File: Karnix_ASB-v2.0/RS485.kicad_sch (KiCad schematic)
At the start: 11 parts, among them U9 MAX487ECSA+

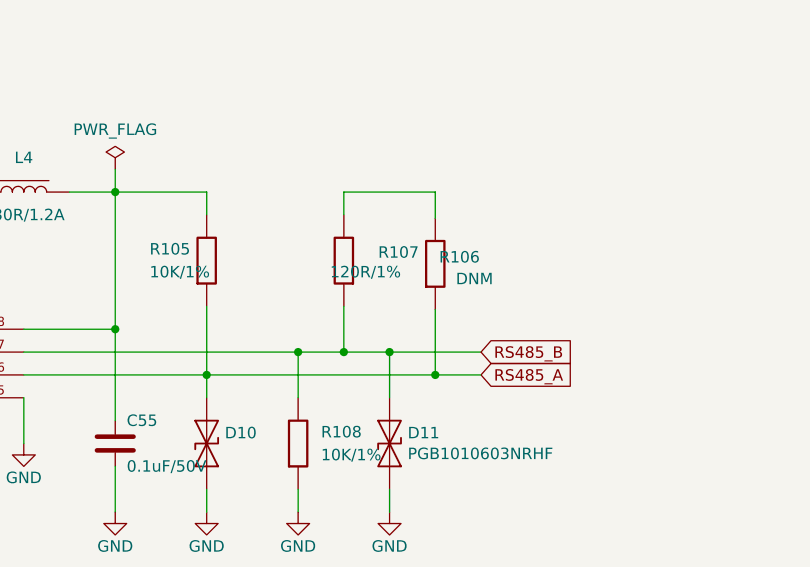
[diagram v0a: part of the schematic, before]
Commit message: V2.0 routing work in progress:
Completed parts:
1. SD-card
2. USB type A connector
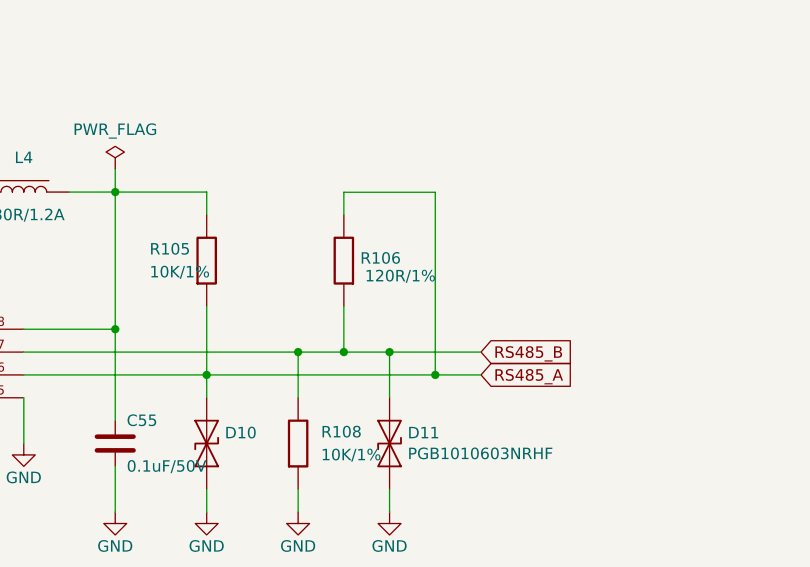
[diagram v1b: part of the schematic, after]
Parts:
- removed R107: DNM, Resistor_SMD:R_0402_1005Metric, symbol Fabmicro:Resistor
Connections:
- net RS485_A: now also R106.1
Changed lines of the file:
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@@
 	(wire
 		(pts
-			(xy 208.026 108.331) (xy 208.026 105.791)
+			(xy 208.026 108.331) (xy 208.026 105.8143)
 		)
 		(stroke
@@
 	(wire
 		(pts
-			(xy 218.186 118.8487) (xy 218.186 126.111)
+			(xy 218.186 105.8143) (xy 218.186 126.111)
 		)
 		(stroke
@@
 	(wire
 		(pts
-			(xy 208.026 105.791) (xy 218.186 105.791)
+			(xy 208.026 105.8143) (xy 218.186 105.8143)
 		)
 		(stroke
@@
 		(pts
 			(xy 177.546 105.791) (xy 182.626 105.791)
-		)
-		(stroke
-			(width 0)
-			(type default)
-		)
-	)
-	(wire
-		(pts
-			(xy 218.186 105.791) (xy 218.186 108.6887)
 		)
 		(stroke
@@
 		(dnp no)
 		(property "Reference" "R106"
-			(at 223.139 113.03 90)
+			(at 214.376 113.157 90)
 			(show_name no)
 			(do_not_autoplace no)
@@
 		)
 		(property "Value" "120R/1%"
-			(at 214.376 114.681 90)
+			(at 218.2495 115.1255 90)
 			(show_name no)
 			(do_not_autoplace no)
@@
 					(unit 1)
 				)
-			)
-		)
-	)
-	(symbol
-		(lib_id "Fabmicro:Resistor")
-		(at 218.186 113.7687 270)
-		(unit 1)
-		(body_style 1)
-		(exclude_from_sim no)
-		(in_bom yes)
-		(on_board yes)
-		(in_pos_files yes)
-		(dnp no)
-		(property "Reference" "R107"
-			(at 211.836 112.4987 90)
-			(show_name no)
-			(do_not_autoplace no)
-			(effects
-				(font
-					(size 1.27 1.27)
-				)
-				(justify left)
-			)
-		)
-		(property "Value" "DNM"
-			(at 220.472 115.443 90)
-			(show_name no)
-			(do_not_autoplace no)
-			(effects
-				(font
-					(size 1.27 1.27)
-				)
-				(justify left)
-			)
-		)
-		(property "Footprint" "Resistor_SMD:R_0402_1005Metric"
-			(at 216.408 113.7687 0)
-			(hide yes)
-			(show_name no)
-			(do_not_autoplace no)
-			(effects
-				(font
-					(size 1.27 1.27)
-				)
-			)
-		)
-		(property "Datasheet" ""
-			(at 218.186 113.7687 90)
-			(hide yes)
-			(show_name no)
-			(do_not_autoplace no)
-			(effects
-				(font
-					(size 1.27 1.27)
-				)
-			)
-		)
-		(property "Description" ""
-			(at 218.186 113.7687 0)
-			(show_name no)
-			(do_not_autoplace no)
-			(effects
-				(font
-					(size 1.27 1.27)
-				)
-			)
-		)
-		(property "Mfr. Part Number" "DNM"
-			(at 218.186 113.7687 0)
-			(hide yes)
-			(show_name no)
-			(do_not_autoplace no)
-			(effects
-				(font
-					(size 1.27 1.27)
-				)
-			)
-		)
-		(property "Supplier" "Fabmicro"
-			(at 218.186 113.7687 0)
-			(hide yes)
-			(show_name no)
-			(do_not_autoplace no)
-			(effects
-				(font
-					(size 1.27 1.27)
-				)
-			)
-		)
-		(property "Field6" ""
-			(at 218.186 113.7687 90)
-			(hide yes)
-			(show_name no)
-			(do_not_autoplace no)
-			(effects
-				(font
-					(size 1.27 1.27)
-				)
-			)
-		)
-		(pin "1"
-		)
-		(pin "2"
-		)
-		(instances
-			(project "Karnix_ASB"
-				(path "/fe37e245-9527-4c72-91fc-09b617a42f73/837bd409-d02c-43f6-9938-fa1825fbf100"
-					(reference "R107")
-					(unit 1)
-				)
